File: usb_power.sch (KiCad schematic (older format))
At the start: 56 parts, among them J1 USB_C16PIN, J2 M20-8770642R, J3 M20-8770642R, Q1 IRLML6402, Q2 BSS214NW, U1 FT230XS, U2 MCP1726-3302ESN, U3 MIC5319-1.8YD5-TR

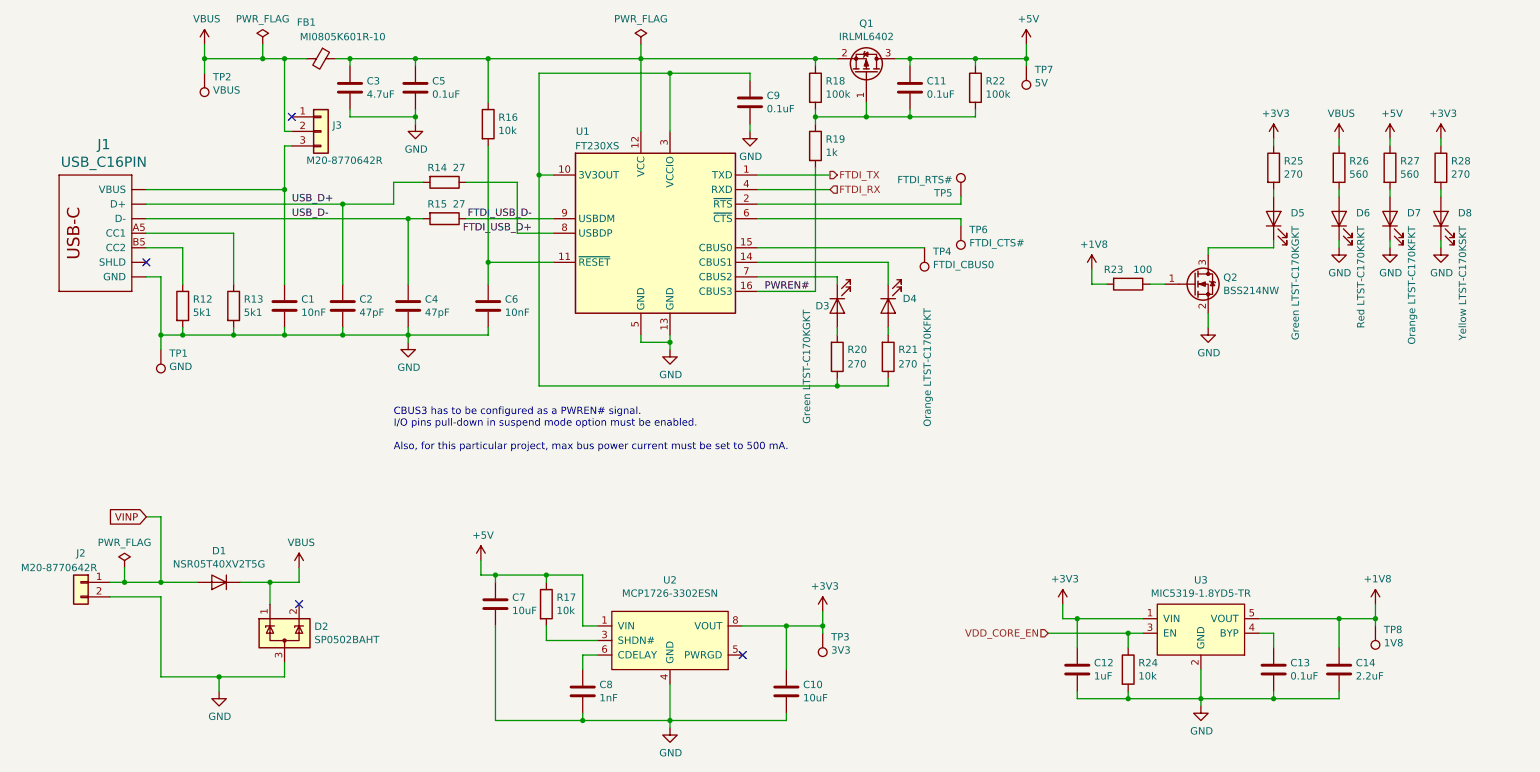
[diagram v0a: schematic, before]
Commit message: Reorder power LEDs in schematics, fix some USB-C DRC errors
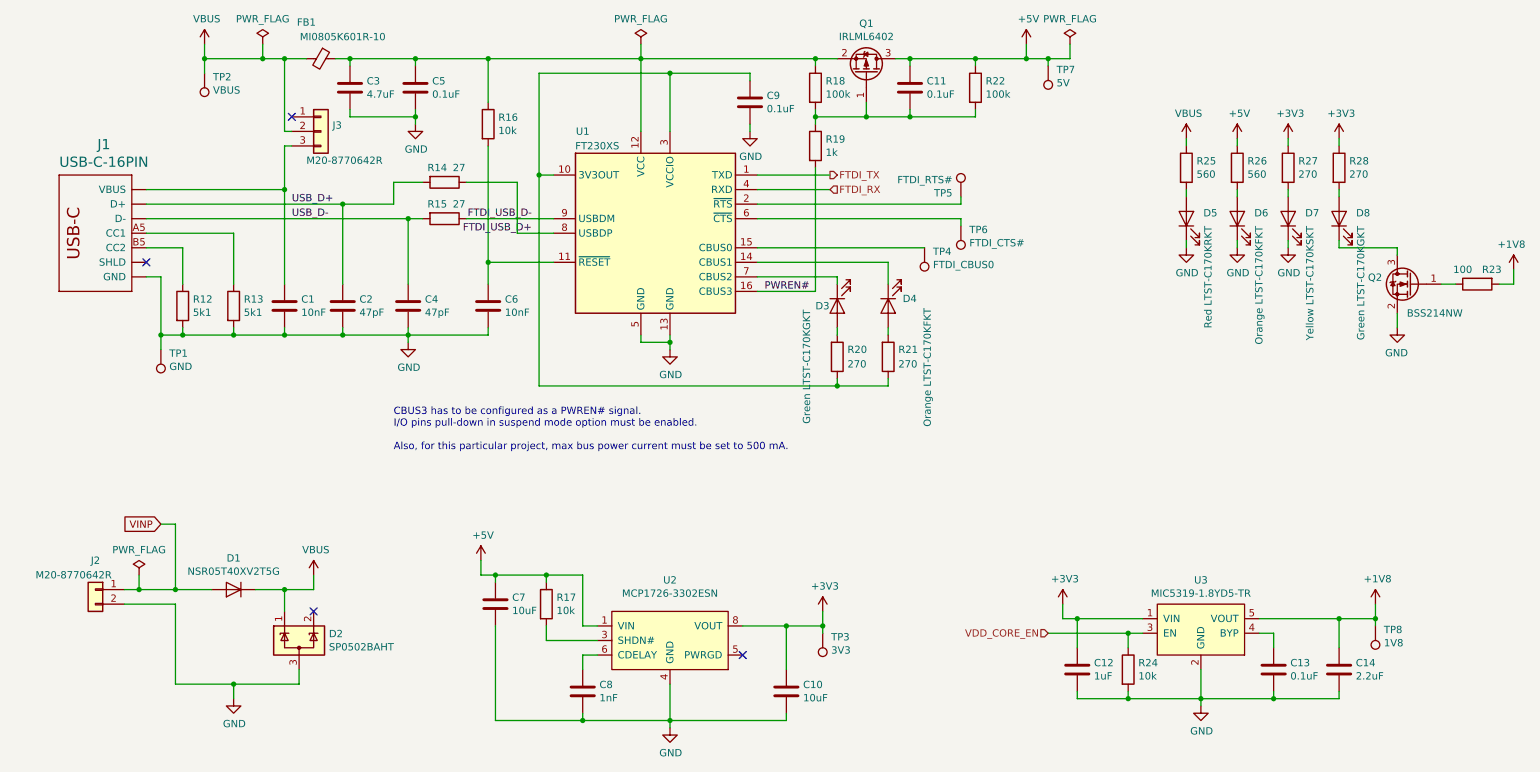
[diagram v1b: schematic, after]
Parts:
- removed J1: USB_C16PIN, USB-C-16pin:USB-C-COM-15111, symbol USB-C-16pin:USB_C16PIN
- added J1: USB-C-16PIN, USB-C-16pin:USB-C-COM-15111, symbol himudev:USB-C-16pin_USB_C16PIN
- renumbered D6 to D5, D7 to D6, D8 to D7, D5 to D8, R26 to R25, R27 to R26, R28 to R27, R25 to R28
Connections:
- net GND: now also J1.GND, J1.GND2 (GND)
- net USB_D+: now also J1.A6 (D+), J1.B6 (D+)
- net USB_D-: now also J1.A7 (D-), J1.B7 (D-)
- net at C1.1, J3.3 (Pin_3): now also J1.VBUS1 (VBUS), J1.VBUS2 (VBUS)
- net at R13.1: now also J1.A5 (CC1)
- net at R12.1: now also J1.B5 (CC2)
- new net: J1.SHLD1 (SHLD), J1.SHLD2 (SHLD), J1.SHLD3 (SHLD), J1.SHLD4 (SHLD), J1.SHLD5 (SHLD), J1.SHLD6 (SHLD), J1.SHLD7 (SHLD), J1.SHLD8 (SHLD)
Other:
- moved on the sheet: D1, D2, D5, D6, D7, D8, J2, Q2, R23, R25, R26, R27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

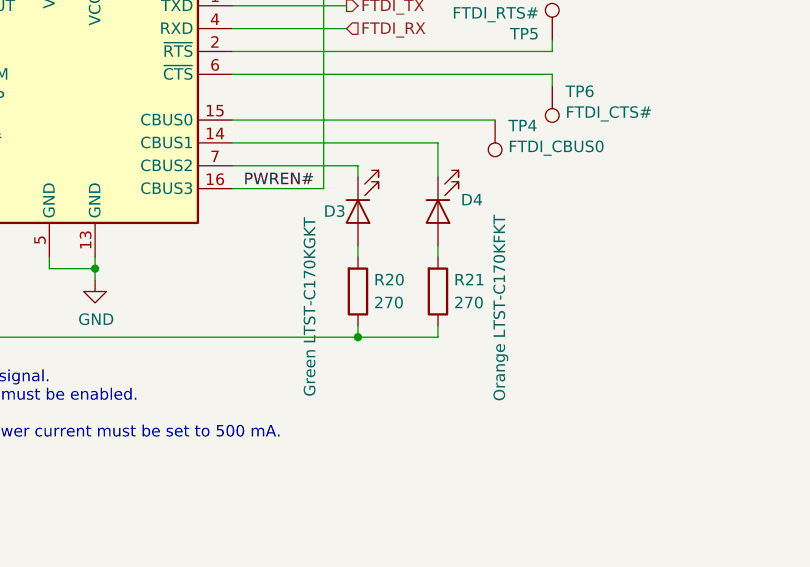
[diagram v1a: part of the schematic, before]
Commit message: Fix: exchange FTDI TX and RX diode colors
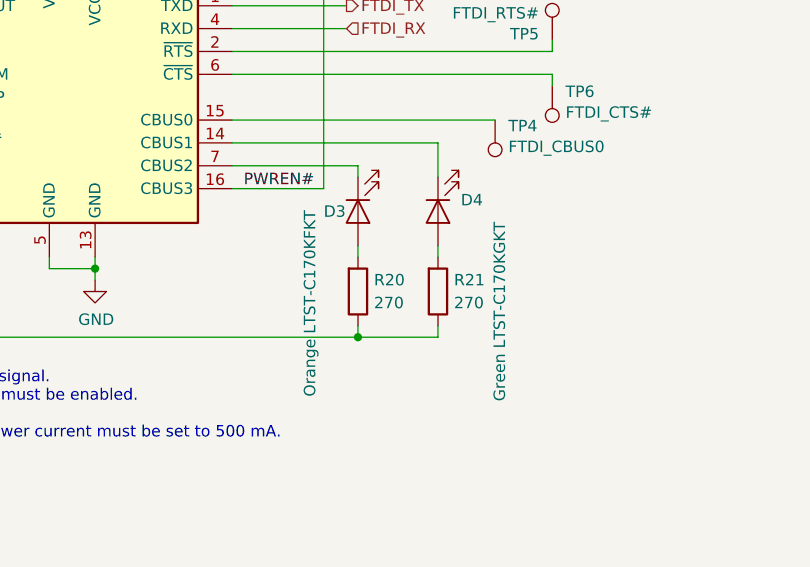
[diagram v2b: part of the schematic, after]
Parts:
- D3: value Green LTST-C170KGKT -> Orange LTST-C170KFKT
- D4: value Orange LTST-C170KFKT -> Green LTST-C170KGKT
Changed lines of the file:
@@
 P 6450 3050
 F 0 "D4" V 6400 2950 50  0000 R CNN
-F 1 "Orange LTST-C170KFKT" H 7280 2780 50  0000 R CNN
+F 1 "Green LTST-C170KGKT" H 7280 2780 50  0000 R CNN
 F 2 "LED_SMD:LED_0805_2012Metric_Pad1.15x1.40mm_HandSolder" H 6450 3050 50  0001 C CNN
 F 3 "~" H 6450 3050 50  0001 C CNN
@@
 P 6100 3050
 F 0 "D3" V 6100 3200 50  0000 R CNN
-F 1 "Green LTST-C170KGKT" H 6910 3260 50  0000 R CNN
+F 1 "Orange LTST-C170KFKT" H 6910 3260 50  0000 R CNN
 F 2 "LED_SMD:LED_0805_2012Metric_Pad1.15x1.40mm_HandSolder" H 6100 3050 50  0001 C CNN
 F 3 "~" H 6100 3050 50  0001 C CNN

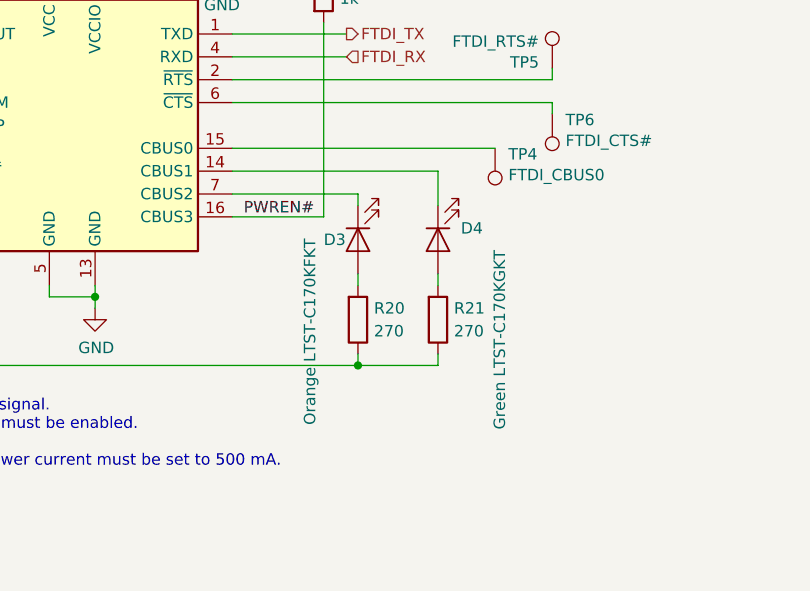
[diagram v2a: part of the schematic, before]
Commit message: Fix FTDI RX/TX diode designator
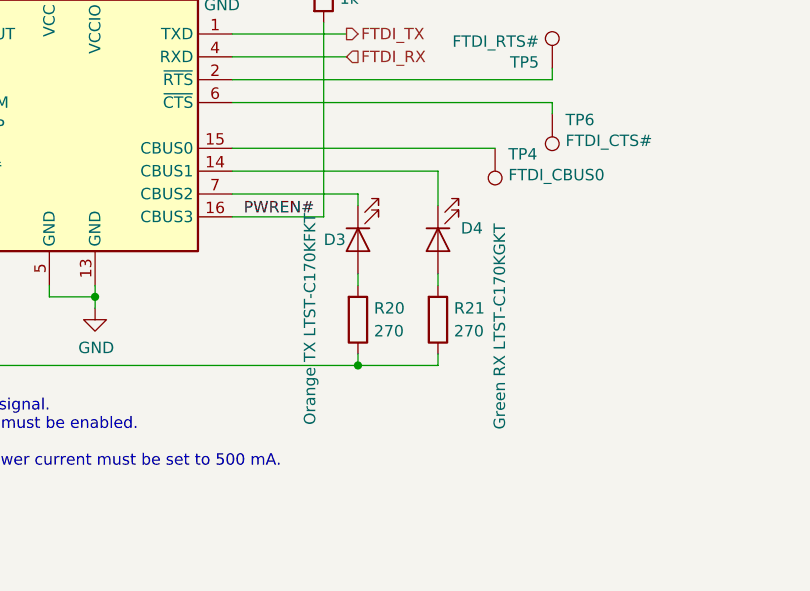
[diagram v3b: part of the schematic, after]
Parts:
- D3: value Orange LTST-C170KFKT -> Orange TX LTST-C170KFKT
- D4: value Green LTST-C170KGKT -> Green RX LTST-C170KGKT
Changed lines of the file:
@@
 Wire Wire Line
 	6450 3250 6450 3200
-$Comp
-L Device:LED D4
-U 1 1 5E1C7665
-P 6450 3050
-F 0 "D4" V 6400 2950 50  0000 R CNN
-F 1 "Green LTST-C170KGKT" H 7280 2780 50  0000 R CNN
-F 2 "LED_SMD:LED_0805_2012Metric_Pad1.15x1.40mm_HandSolder" H 6450 3050 50  0001 C CNN
-F 3 "~" H 6450 3050 50  0001 C CNN
-	1    6450 3050
-	0    -1   1    0
-$EndComp
 Wire Wire Line
 	6450 3600 6450 3550
@@
 P 6100 3050
 F 0 "D3" V 6100 3200 50  0000 R CNN
-F 1 "Orange LTST-C170KFKT" H 6910 3260 50  0000 R CNN
+F 1 "Orange TX LTST-C170KFKT" H 6910 3260 50  0000 R CNN
 F 2 "LED_SMD:LED_0805_2012Metric_Pad1.15x1.40mm_HandSolder" H 6100 3050 50  0001 C CNN
 F 3 "~" H 6100 3050 50  0001 C CNN
@@
 	1    0    0    -1
 $EndComp
+$Comp
+L Device:LED D4
+U 1 1 5E1C7665
+P 6450 3050
+F 0 "D4" V 6400 2950 50  0000 R CNN
+F 1 "Green RX LTST-C170KGKT" H 7280 2780 50  0000 R CNN
+F 2 "LED_SMD:LED_0805_2012Metric_Pad1.15x1.40mm_HandSolder" H 6450 3050 50  0001 C CNN
+F 3 "~" H 6450 3050 50  0001 C CNN
+	1    6450 3050
+	0    -1   1    0
+$EndComp
 $EndSCHEMATC

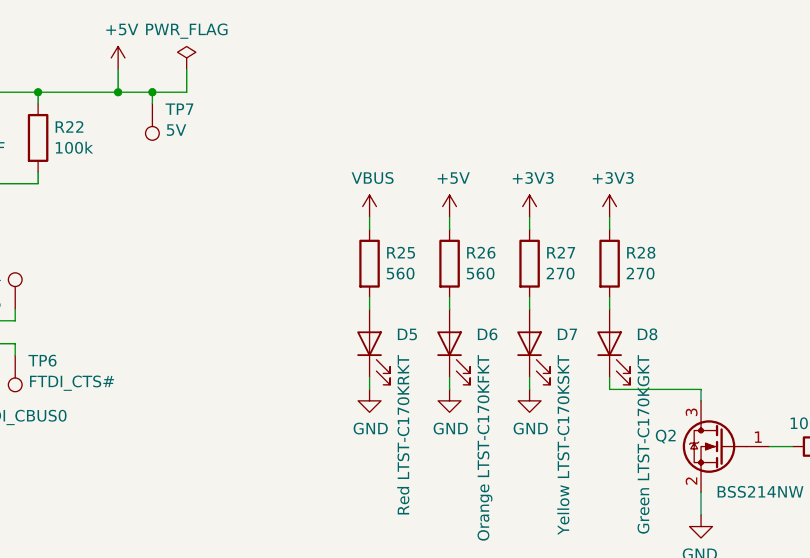
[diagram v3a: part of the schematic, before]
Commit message: Change resistor values to adjust LED brightness
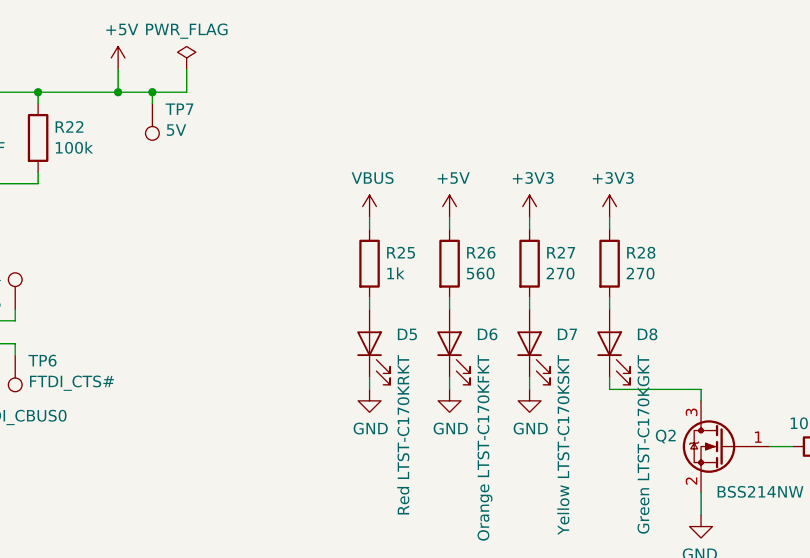
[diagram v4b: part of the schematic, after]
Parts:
- R25: value 560 -> 1k
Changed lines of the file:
@@
 P 8500 2100
 F 0 "R25" H 8570 2146 50  0000 L CNN
-F 1 "560" H 8570 2055 50  0000 L CNN
+F 1 "1k" H 8570 2055 50  0000 L CNN
 F 2 "Resistor_SMD:R_0603_1608Metric_Pad1.05x0.95mm_HandSolder" V 8430 2100 50  0001 C CNN
 F 3 "~" H 8500 2100 50  0001 C CNN

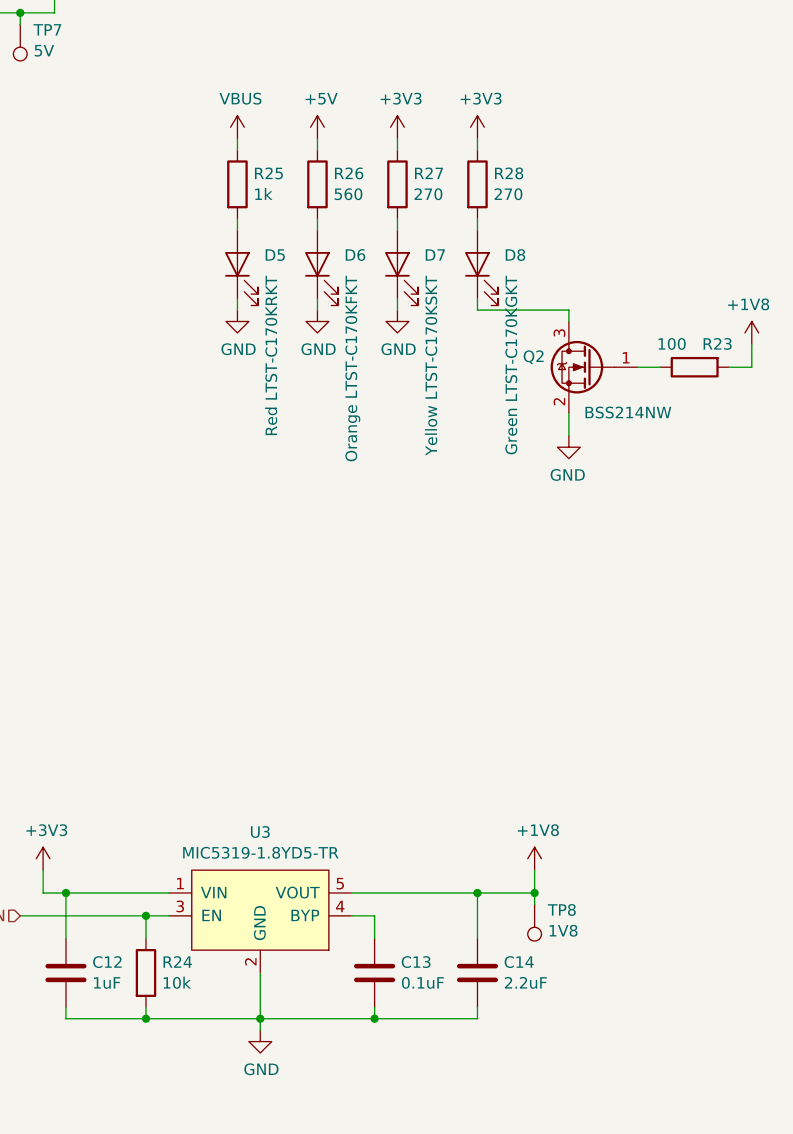
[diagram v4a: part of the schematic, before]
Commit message: Add 10k pull-downs on MCU LED outputs, improve layout
Pushed few traces, fixed DRC issue on one of the vias.
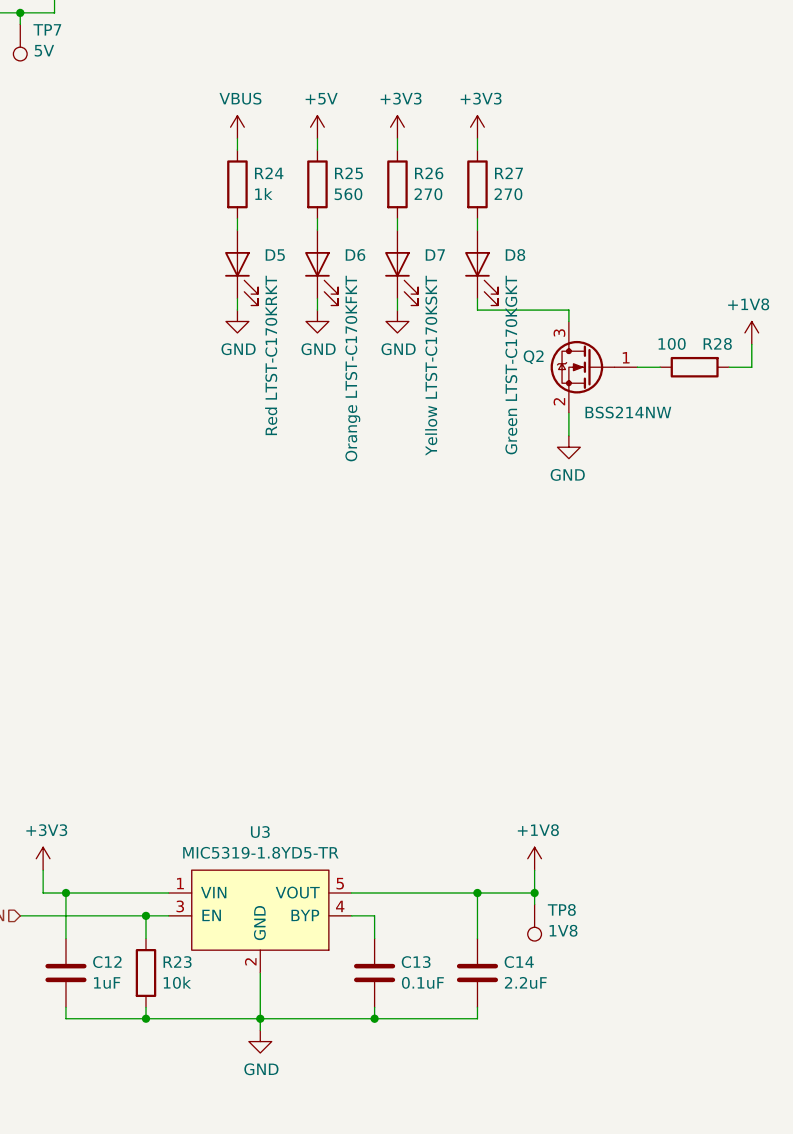
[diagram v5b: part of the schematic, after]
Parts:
- renumbered R24 to R23, R25 to R24, R26 to R25, R27 to R26, R28 to R27, R23 to R28
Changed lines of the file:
@@
 $EndDescr
 $Comp
-L power:VBUS #PWR017
+L power:VBUS #PWR013
 U 1 1 5DFF0B39
 P 8500 1900
-F 0 "#PWR017" H 8500 1750 50  0001 C CNN
+F 0 "#PWR013" H 8500 1750 50  0001 C CNN
 F 1 "VBUS" H 8515 2073 50  0000 C CNN
 F 2 "" H 8500 1900 50  0001 C CNN
@@
 $EndComp
 $Comp
-L power:+5V #PWR020
+L power:+5V #PWR016
 U 1 1 5DFF12F3
 P 8850 1900
-F 0 "#PWR020" H 8850 1750 50  0001 C CNN
+F 0 "#PWR016" H 8850 1750 50  0001 C CNN
 F 1 "+5V" H 8865 2073 50  0000 C CNN
 F 2 "" H 8850 1900 50  0001 C CNN
@@
 $EndComp
 $Comp
-L Device:R R25
+L Device:R R24
 U 1 1 5DFF1834
 P 8500 2100
-F 0 "R25" H 8570 2146 50  0000 L CNN
+F 0 "R24" H 8570 2146 50  0000 L CNN
 F 1 "1k" H 8570 2055 50  0000 L CNN
 F 2 "Resistor_SMD:R_0603_1608Metric_Pad1.05x0.95mm_HandSolder" V 8430 2100 50  0001 C CNN
@@
 $EndComp
 $Comp
-L Device:R R26
+L Device:R R25
 U 1 1 5DFF24B7
 P 8850 2100
-F 0 "R26" H 8920 2146 50  0000 L CNN
+F 0 "R25" H 8920 2146 50  0000 L CNN
 F 1 "560" H 8920 2055 50  0000 L CNN
 F 2 "Resistor_SMD:R_0603_1608Metric_Pad1.05x0.95mm_HandSolder" V 8780 2100 50  0001 C CNN
@@
 	8500 1900 8500 1950
 $Comp
-L power:GND #PWR021
+L power:GND #PWR017
 U 1 1 5DFF81F2
 P 8850 2650
-F 0 "#PWR021" H 8850 2400 50  0001 C CNN
+F 0 "#PWR017" H 8850 2400 50  0001 C CNN
 F 1 "GND" H 8855 2477 50  0000 C CNN
 F 2 "" H 8850 2650 50  0001 C CNN
@@
 $EndComp
 $Comp
-L power:GND #PWR018
+L power:GND #PWR014
 U 1 1 5DFF8CF3
 P 8500 2650
-F 0 "#PWR018" H 8500 2400 50  0001 C CNN
+F 0 "#PWR014" H 8500 2400 50  0001 C CNN
 F 1 "GND" H 8505 2477 50  0000 C CNN
 F 2 "" H 8500 2650 50  0001 C CNN
@@
 	8500 2250 8500 2300
 $Comp
-L Device:R R27
+L Device:R R26
 U 1 1 5E003891
 P 9200 2100
-F 0 "R27" H 9270 2146 50  0000 L CNN
+F 0 "R26" H 9270 2146 50  0000 L CNN
 F 1 "270" H 9270 2055 50  0000 L CNN
 F 2 "Resistor_SMD:R_0603_1608Metric_Pad1.05x0.95mm_HandSolder" V 9130 2100 50  0001 C CNN
@@
 $EndComp
 $Comp
-L power:GND #PWR023
+L power:GND #PWR019
 U 1 1 5E0038B1
 P 9200 2650
-F 0 "#PWR023" H 9200 2400 50  0001 C CNN
+F 0 "#PWR019" H 9200 2400 50  0001 C CNN
 F 1 "GND" H 9205 2477 50  0000 C CNN
 F 2 "" H 9200 2650 50  0001 C CNN
@@
 	9200 2250 9200 2300
 $Comp
-L power:+3V3 #PWR022
+L power:+3V3 #PWR018
 U 1 1 5E006055
 P 9200 1900
-F 0 "#PWR022" H 9200 1750 50  0001 C CNN
+F 0 "#PWR018" H 9200 1750 50  0001 C CNN
 F 1 "+3V3" H 9215 2073 50  0000 C CNN
 F 2 "" H 9200 1900 50  0001 C CNN
@@
 $EndComp
 $Comp
-L Device:R R24
+L Device:R R23
 U 1 1 5E07197E
 P 8100 5550
-F 0 "R24" H 8170 5596 50  0000 L CNN
+F 0 "R23" H 8170 5596 50  0000 L CNN
 F 1 "10k" H 8170 5505 50  0000 L CNN
 F 2 "Resistor_SMD:R_0603_1608Metric_Pad1.05x0.95mm_HandSolder" V 8030 5550 50  0001 C CNN
@@
 	9550 5200 9550 5400
 $Comp
-L power:GND #PWR014
+L power:GND #PWR015
 U 1 1 5E0A77ED
 P 8600 5800
-F 0 "#PWR014" H 8600 5550 50  0001 C CNN
+F 0 "#PWR015" H 8600 5550 50  0001 C CNN
 F 1 "GND" H 8605 5627 50  0000 C CNN
 F 2 "" H 8600 5800 50  0001 C CNN
@@
 	8600 5800 8600 5750
 $Comp
-L power:+1V8 #PWR019
+L power:+1V8 #PWR021
 U 1 1 5E0ADC80
 P 9800 5100
-F 0 "#PWR019" H 9800 4950 50  0001 C CNN
+F 0 "#PWR021" H 9800 4950 50  0001 C CNN
 F 1 "+1V8" H 9815 5273 50  0000 C CNN
 F 2 "" H 9800 5100 50  0001 C CNN
@@
 $EndComp
 $Comp
-L power:+3V3 #PWR016
+L power:+3V3 #PWR020
 U 1 1 5E3657BB
 P 9550 1900
-F 0 "#PWR016" H 9550 1750 50  0001 C CNN
+F 0 "#PWR020" H 9550 1750 50  0001 C CNN
 F 1 "+3V3" H 9565 2073 50  0000 C CNN
 F 2 "" H 9550 1900 50  0001 C CNN
@@
 $EndComp
 $Comp
-L Device:R R28
+L Device:R R27
 U 1 1 5E003897
 P 9550 2100
-F 0 "R28" H 9620 2146 50  0000 L CNN
+F 0 "R27" H 9620 2146 50  0000 L CNN
 F 1 "270" H 9620 2055 50  0000 L CNN
 F 2 "Resistor_SMD:R_0603_1608Metric_Pad1.05x0.95mm_HandSolder" V 9480 2100 50  0001 C CNN
@@
 FTDI_USB_D-
 $Comp
-L power:+1V8 #PWR013
+L power:+1V8 #PWR023
 U 1 1 5E36EBB9
 P 10750 2800
-F 0 "#PWR013" H 10750 2650 50  0001 C CNN
+F 0 "#PWR023" H 10750 2650 50  0001 C CNN
 F 1 "+1V8" H 10765 2973 50  0000 C CNN
 F 2 "" H 10750 2800 50  0001 C CNN
@@
 $EndComp
 $Comp
-L Device:R R23
+L Device:R R28
 U 1 1 5E00107A
 P 10500 2900
-F 0 "R23" V 10400 2800 50  0000 C CNN
+F 0 "R28" V 10400 2800 50  0000 C CNN
 F 1 "100" V 10400 3000 50  0000 C CNN
 F 2 "Resistor_SMD:R_0603_1608Metric_Pad1.05x0.95mm_HandSolder" V 10430 2900 50  0001 C CNN
@@
 $EndComp
 $Comp
-L power:GND #PWR015
+L power:GND #PWR022
 U 1 1 5E0038AB
 P 9950 3200
-F 0 "#PWR015" H 9950 2950 50  0001 C CNN
+F 0 "#PWR022" H 9950 2950 50  0001 C CNN
 F 1 "GND" H 9955 3027 50  0000 C CNN
 F 2 "" H 9950 3200 50  0001 C CNN
@@
 $EndComp
 $Comp
-L power:PWR_FLAG #FLG0101
+L power:PWR_FLAG #FLG04
 U 1 1 5E960C6C
 P 7700 1250
-F 0 "#FLG0101" H 7700 1325 50  0001 C CNN
+F 0 "#FLG04" H 7700 1325 50  0001 C CNN
 F 1 "PWR_FLAG" H 7700 1423 50  0000 C CNN
 F 2 "" H 7700 1250 50  0001 C CNN
